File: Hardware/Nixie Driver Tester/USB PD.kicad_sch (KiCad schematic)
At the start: 10 parts, among them J2 UJC-HP-3-SMT-TR

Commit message: Using a STM32 instead of a PIC
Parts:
- S1: footprint SamacSys_Parts:SLW1116297AD -> Switch_:SLW1116297AD
- U2: value ~ -> (none)

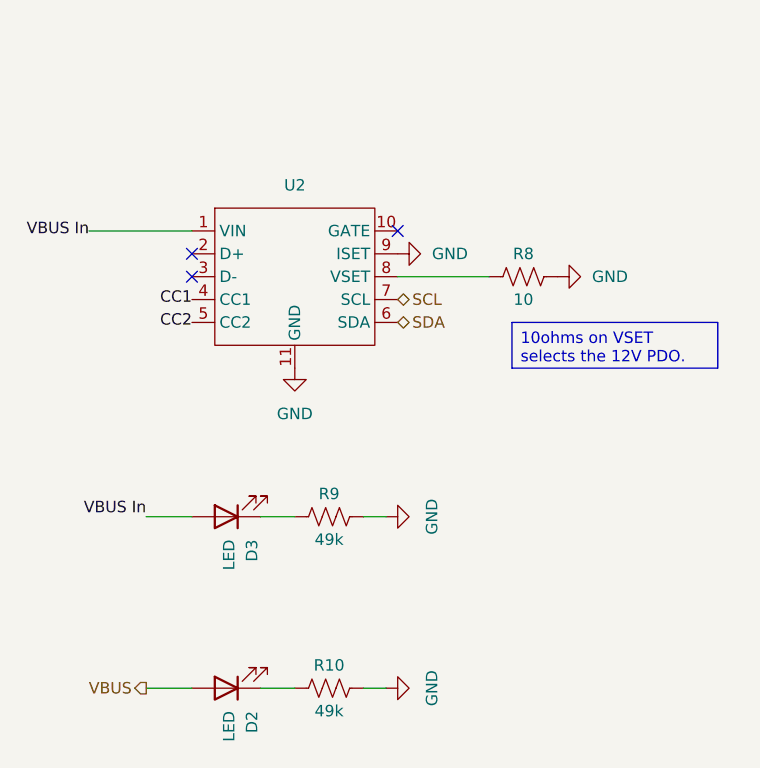
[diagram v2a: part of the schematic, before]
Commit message: Switch mode 3.3V and SMD inductor
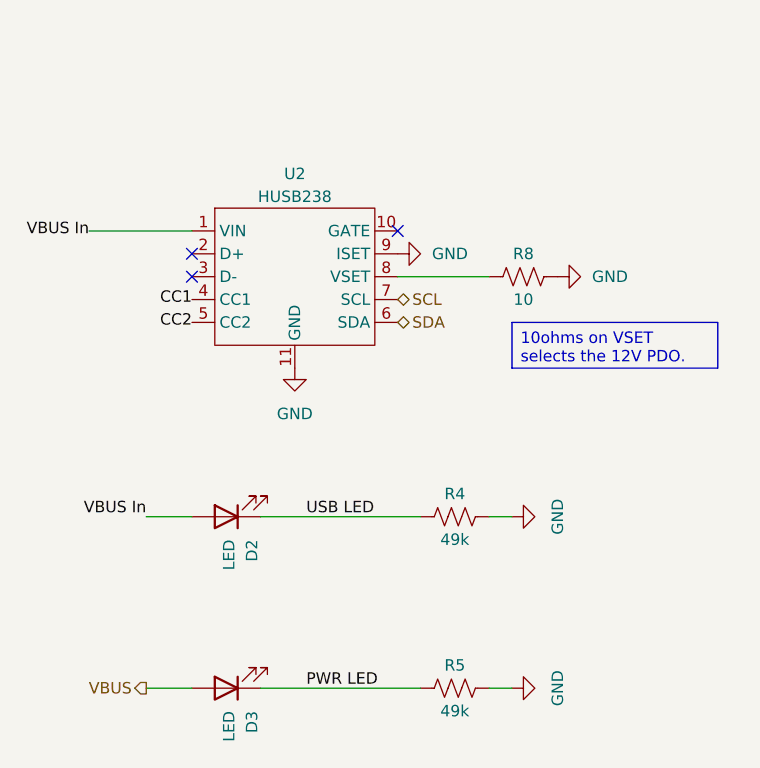
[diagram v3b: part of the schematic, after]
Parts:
- U2: value (none) -> HUSB238
- renumbered D3 to D2, D2 to D3, J2 to J3, R9 to R4, R10 to R5
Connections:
- net PWR LED: now reaches D3.1 (K), R5.1
- net USB LED: now reaches D2.1 (K), R4.1
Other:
- moved on the sheet: R4, R5

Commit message: Added test points
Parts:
- added TP7: GND, TestPoint:TestPoint_Keystone_5015_Micro_Mini, symbol Connector:TestPoint
- added TP8: VBUS, TestPoint:TestPoint_Keystone_5015_Micro_Mini, symbol Connector:TestPoint
- renumbered R6 to R4, R7 to R5, R4 to R6, R5 to R7
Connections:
- net GND: now also TP7.1
- net VBUS In: now also TP8.1

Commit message: New driver interface
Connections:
- net VBUS: now also TP8.1
- net VBUS In: no longer TP8.1
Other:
- moved on the sheet: TP8
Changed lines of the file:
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@@
+	)
+	(junction
+		(at 107.95 83.82)
+		(diameter 0)
+		(color 0 0 0 0)
 	)
 	(junction
@@
 	)
 	(junction
-		(at 147.32 91.44)
-		(diameter 0)
-		(color 0 0 0 0)
-	)
-	(junction
 		(at 101.6 83.82)
 		(diameter 0)
@@
 	(wire
 		(pts
-			(xy 101.6 83.82) (xy 120.65 83.82)
+			(xy 101.6 83.82) (xy 107.95 83.82)
 		)
 		(stroke
@@
 	(wire
 		(pts
-			(xy 140.97 91.44) (xy 147.32 91.44)
+			(xy 107.95 83.82) (xy 120.65 83.82)
+		)
+		(stroke
+			(width 0)
+			(type default)
+		)
+	)
+	(wire
+		(pts
+			(xy 140.97 91.44) (xy 152.4 91.44)
 		)
 		(stroke
@@
 		(pts
 			(xy 132.08 57.15) (xy 127 57.15)
-		)
-		(stroke
-			(width 0)
-			(type default)
-		)
-	)
-	(wire
-		(pts
-			(xy 147.32 91.44) (xy 152.4 91.44)
 		)
 		(stroke
@@
 	(symbol
 		(lib_id "Connector:TestPoint")
-		(at 147.32 91.44 0)
+		(at 107.95 83.82 0)
 		(unit 1)
 		(body_style 1)
@@
 		(dnp no)
 		(property "Reference" "TP8"
-			(at 147.32 86.36 0)
+			(at 107.95 78.74 0)
 			(show_name no)
 			(do_not_autoplace no)
@@
 		)
 		(property "Value" "VBUS"
-			(at 149.86 89.4079 0)
+			(at 110.49 81.7879 0)
 			(hide yes)
 			(show_name no)
@@
 		)
 		(property "Footprint" "TestPoint:TestPoint_Keystone_5015_Micro_Mini"
-			(at 152.4 91.44 0)
+			(at 113.03 83.82 0)
 			(hide yes)
 			(show_name no)
@@
 		)
 		(property "Datasheet" ""
-			(at 152.4 91.44 0)
+			(at 113.03 83.82 0)
 			(hide yes)
 			(show_name no)
@@
 		)
 		(property "Description" "test point"
-			(at 147.32 91.44 0)
-			(hide yes)
-			(show_name no)
+			(at 107.95 83.82 0)
+			(hide yes)
+			(show_name no)
